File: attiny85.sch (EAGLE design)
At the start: 8 parts, among them U1 TINY85-20-DIP

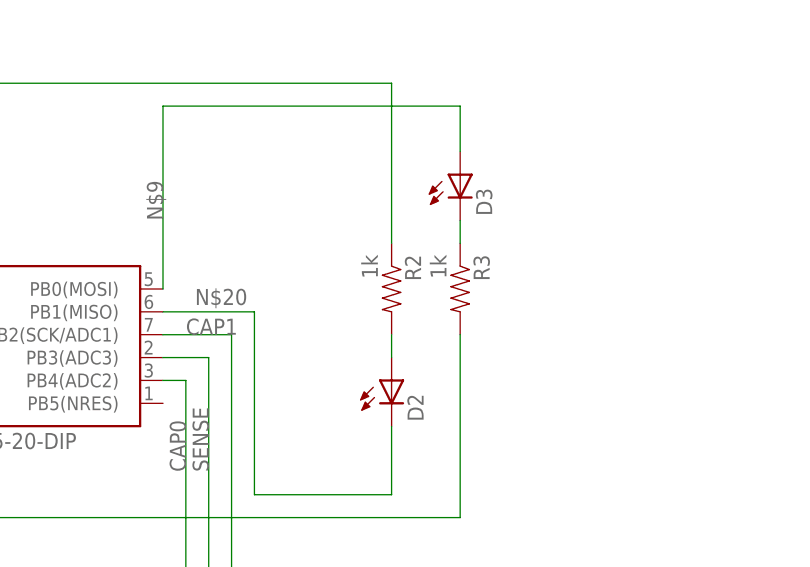
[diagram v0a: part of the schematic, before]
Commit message: Updating resistor values
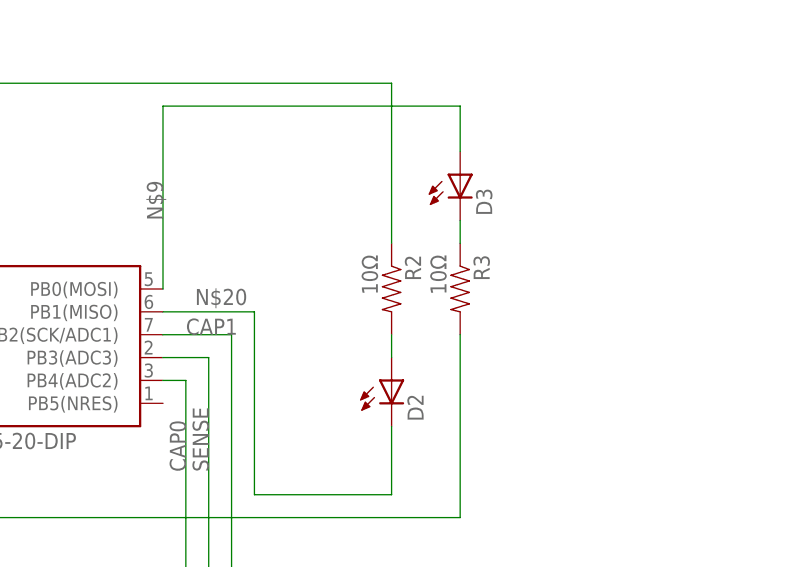
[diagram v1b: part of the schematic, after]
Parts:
- R2, R3: value 1k -> 10Ω
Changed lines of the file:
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@@
 <part name="FRAME1" library="frames" deviceset="TABL_L" device=""/>
 <part name="U1" library="SparkFun-DigitalIC" deviceset="ATTINY45" device="TINY85-20-DIP" value="TINY85-20-DIP"/>
-<part name="R2" library="SparkFun-Resistors" deviceset="1KOHM-1/4W-5%(PTH)" device="" value="1k"/>
+<part name="R2" library="SparkFun-Resistors" deviceset="1KOHM-1/4W-5%(PTH)" device="" value="10Ω"/>
 <part name="D2" library="LED" deviceset="LED" device="5MM"/>
-<part name="R3" library="SparkFun-Resistors" deviceset="1KOHM-1/4W-5%(PTH)" device="" value="1k"/>
+<part name="R3" library="SparkFun-Resistors" deviceset="1KOHM-1/4W-5%(PTH)" device="" value="10Ω"/>
 <part name="D3" library="LED" deviceset="LED" device="5MM"/>
 <part name="R17" library="SparkFun-Resistors" deviceset="1KOHM-1/4W-5%(PTH)" device="" value="1M"/>

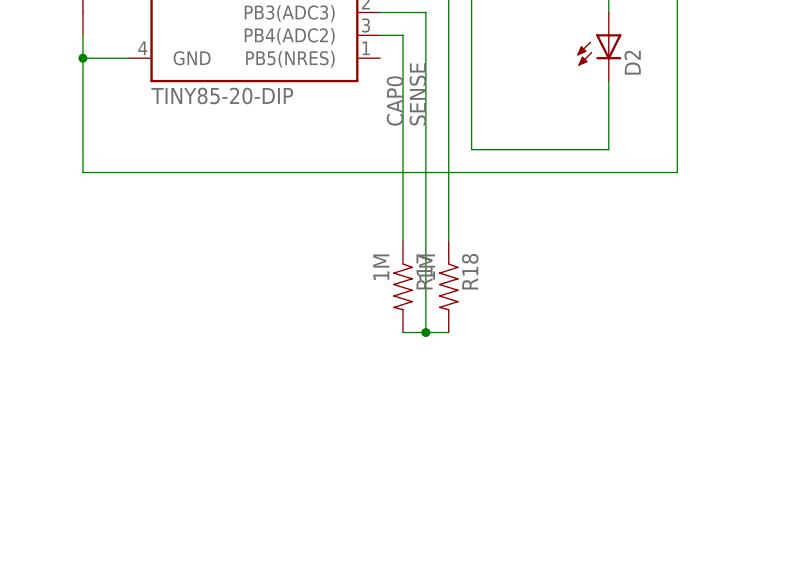
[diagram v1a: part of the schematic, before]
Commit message: More fixing of values
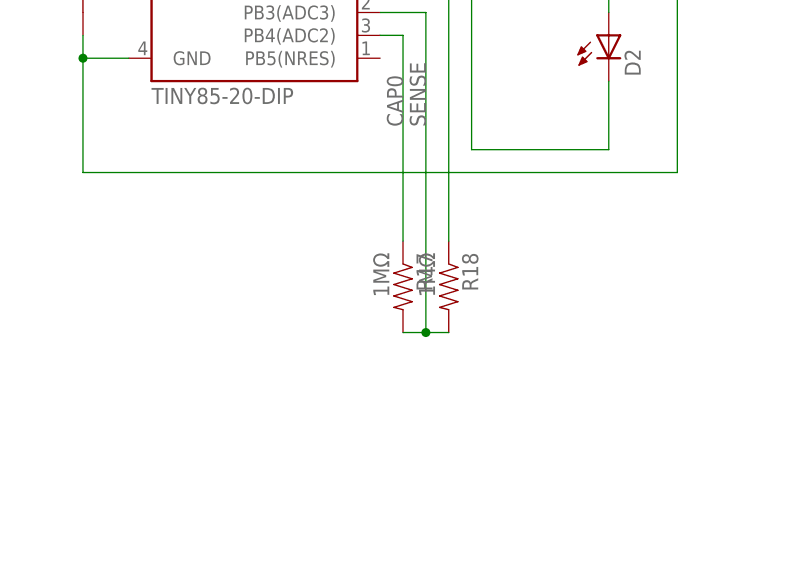
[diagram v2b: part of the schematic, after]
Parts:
- R17, R18: value 1M -> 1MΩ
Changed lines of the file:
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@@
 <part name="R3" library="SparkFun-Resistors" deviceset="1KOHM-1/4W-5%(PTH)" device="" value="10Ω"/>
 <part name="D3" library="LED" deviceset="LED" device="5MM"/>
-<part name="R17" library="SparkFun-Resistors" deviceset="1KOHM-1/4W-5%(PTH)" device="" value="1M"/>
-<part name="R18" library="SparkFun-Resistors" deviceset="1KOHM-1/4W-5%(PTH)" device="" value="1M"/>
+<part name="R17" library="SparkFun-Resistors" deviceset="1KOHM-1/4W-5%(PTH)" device="" value="1MΩ"/>
+<part name="R18" library="SparkFun-Resistors" deviceset="1KOHM-1/4W-5%(PTH)" device="" value="1MΩ"/>
 <part name="BAT1" library="adafruit-john modded" deviceset="CR2032" device="THM"/>
 </parts>
